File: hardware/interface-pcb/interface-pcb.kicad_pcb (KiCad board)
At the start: 2 copper layers, 90 x 75 mm, 102 parts, among them J1 Siedle bus Ta/Tb, J2 ext. 5V, Q1 IRFR120N, Q2 BC846B, Q3 BCP56-16, Q4 BCP56-16, Q5 BC846B, SW1 setup, U1 R-78CK5.0-0.5, U2 LM393, U3 ES8311, U4 MCP6002, U5 ESP32 D1 Mini

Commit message: Show the D1 Mini in the 3D view
The 3D view showed the empty sockets only, so the case design had no
module to work around. MK1 is a mechanical footprint locked on U5's
position that carries just a 3D model of the AZ-Delivery ESP32 D1 Mini:
no pads, not in the schematic, BOM or position files, footprint type
Unspecified. That makes it switchable: the 3D viewer's Unspecified
models toggle shows the board with or without it, and the STEP export
drops it with --no-unspecified. Putting the model into U5's own
footprint would instead need a footprint edit for every toggle.

tools/d1_mini_model.py builds the model from nominal dimensions (AZ-
Delivery's product page and photos): the board, the WROOM-32 with its
antenna at the edge, micro-USB, reset button, CP2104 and the male
headers, the top at about 15.3 mm above our board. The parameters take
the caliper measurements later. Both model scripts now share
tools/step_util.py for writing coloured STEP files.

DRC with schematic parity: 0 violations, 0 unconnected items, 0 parity
issues, as before.

Co-Authored-By: Claude Opus 5.5 <noreply@anthropic.com>
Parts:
- added MK1: ESP32 D1 Mini, 3D only, gateway:D1_Mini_ESP32_Module_3D, F.Cu at (116.0, 71.2)
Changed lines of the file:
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@@
+		)
+	)
+	(footprint "gateway:D1_Mini_ESP32_Module_3D"
+		(locked yes)
+		(layer "F.Cu")
+		(at 116 71.2)
+		(descr "3D model of the AZ-Delivery ESP32 D1 Mini plugged into the D1_Mini_ESP32_Socket footprint. Place at the socket footprint's origin. No pads, not in the schematic, BOM or position files; type Unspecified, so the 3D viewer can hide it and STEP export drops it with --no-unspecified.")
+		(tags "ESP32 D1 Mini 3D mechanical")
+		(property "Reference" "MK1"
+			(at 0 -22.5 0)
+			(layer "F.Fab")
+			(hide yes)
+			(effects
+				(font
+					(size 1 1)
+					(thickness 0.15)
+				)
+			)
+		)
+		(property "Value" "ESP32 D1 Mini, 3D only"
+			(at 0 21.5 0)
+			(layer "F.Fab")
+			(hide yes)
+			(effects
+				(font
+					(size 1 1)
+					(thickness 0.15)
+				)
+			)
+		)
+		(property "Datasheet" "https://www.az-delivery.de/en/products/esp32-d1-mini"
+			(at 0 0 0)
+			(layer "F.Fab")
+			(hide yes)
+			(effects
+				(font
+					(size 1.27 1.27)
+				)
+			)
+		)
+		(property "Description" "Mechanical: the D1 Mini module for the 3D view and the case design"
+			(at 0 0 0)
+			(layer "F.Fab")
+			(hide yes)
+			(effects
+				(font
+					(size 1.27 1.27)
+				)
+			)
+		)
+		(attr board_only exclude_from_pos_files exclude_from_bom)
+		(duplicate_pad_numbers_are_jumpers no)
+		(embedded_fonts no)
+		(model "${KIPRJMOD}/gateway.3dshapes/ESP32_D1_Mini_AZ-Delivery.step"
+			(offset
+				(xyz 0 0 0)
+			)
+			(scale
+				(xyz 1 1 1)
+			)
+			(rotate
+				(xyz 0 0 0)
+			)
 		)
 	)

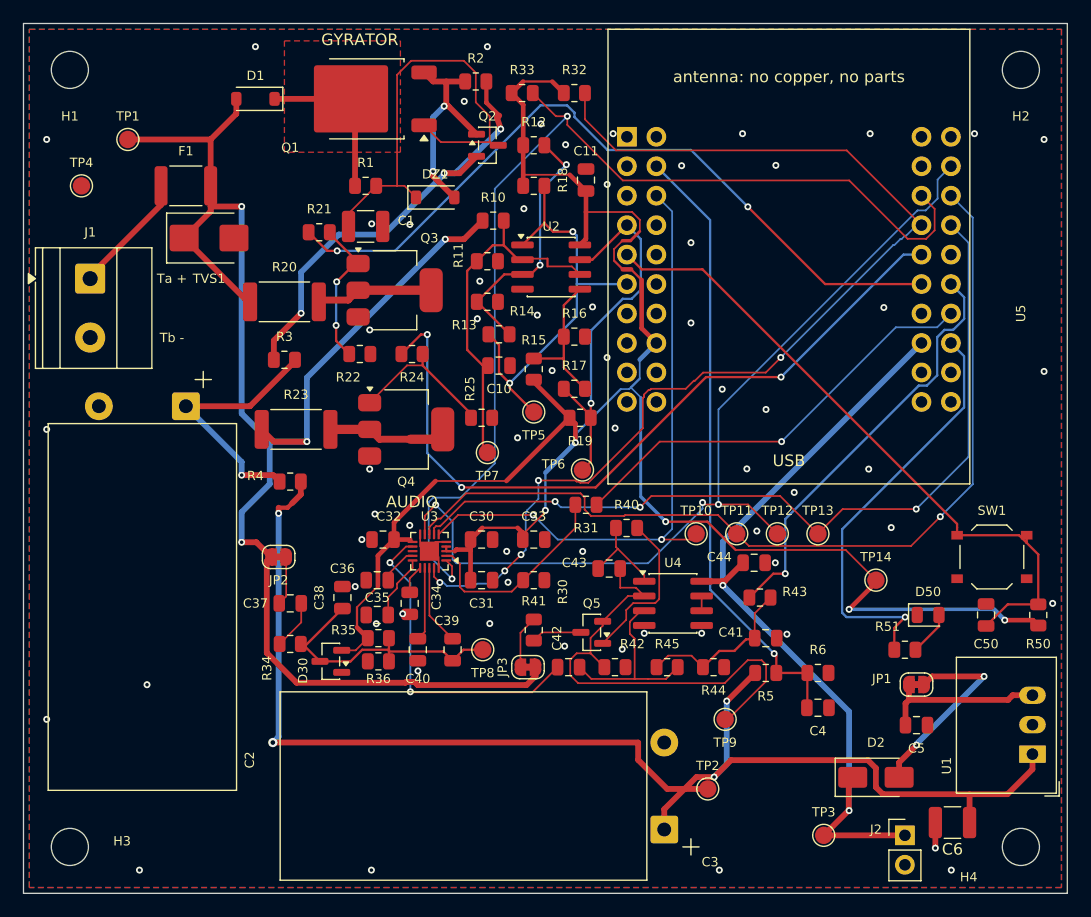
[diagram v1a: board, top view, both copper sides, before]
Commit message: Use 1000 uF / 35 V for C2 and C3
The 2200 uF / 50 V capacitors were the tallest parts after the D1 Mini.
Without load they sit about 4 V below the bus, 28 V while it rings at
32 V, so 35 V parts are enough; and smaller capacitors filter the Wi-Fi
bursts as well when R3 and R4 grow with them. C2 and C3 become
1000 uF / 35 V (13 x 20 mm, LCSC C10749), R3 and R4 33 and 39 ohms.

The decision comes before the bus measurements on purpose: if the bus
rings above 32 V, the 2200 uF / 50 V parts with 15 and 18 ohms go back
in, and the 16 mm footprint and model stay in the library for that.

Both variants get the change. A new lying footprint (5 mm pitch) and its
3D model replace the 16 mm ones on the boards; pad 1 stays put, pad 2
moves 2.5 mm closer and lands on C3's VOUT feed, which now runs straight
down to pad 1's track. gyrator.cir takes the new values: 3.2 s to 14 V,
VOUT 19.2 V, a 0.83 V dip during a frame, 130-170 kohm toward the bus
at speech frequencies.

ERC: no violations in both projects. DRC with schematic parity on the
D1 Mini board: 0 violations, 0 unconnected items, 0 parity issues. The
S3 board shows only the parity issues of its pending layout.

Co-Authored-By: Claude Opus 5.5 <noreply@anthropic.com>
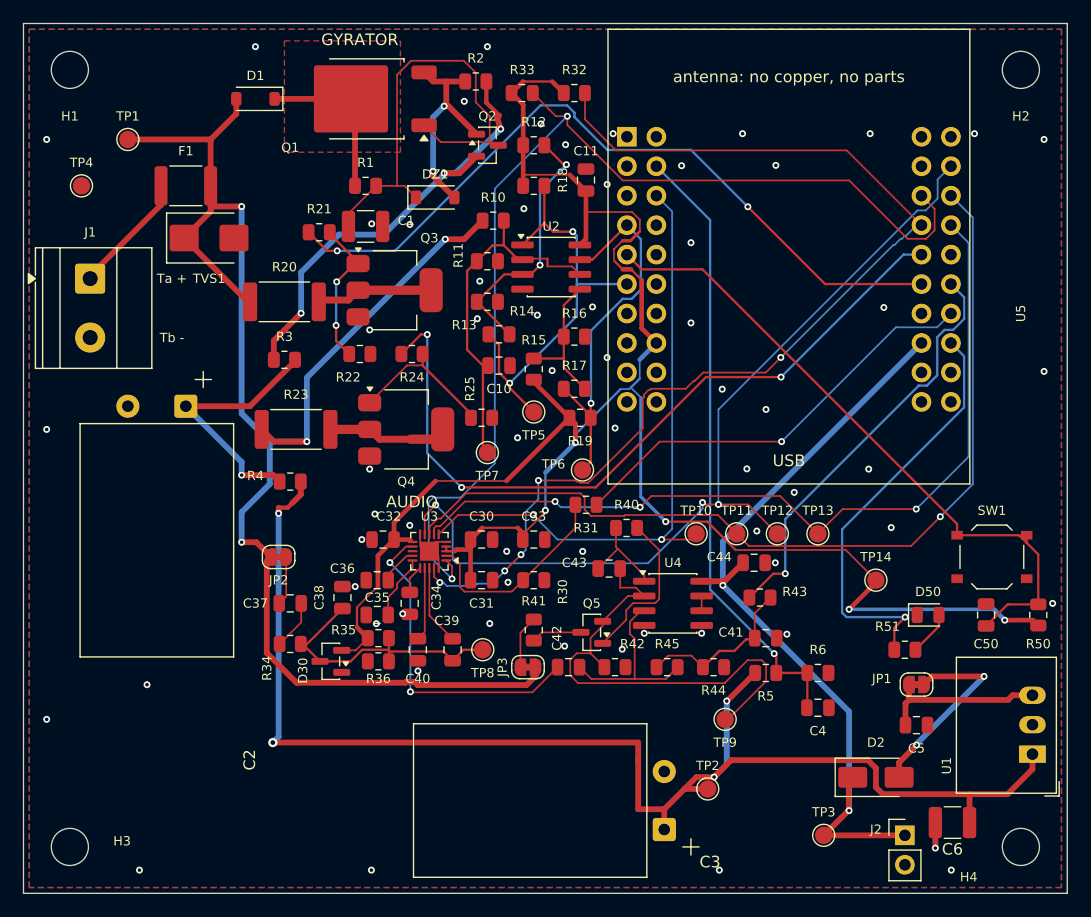
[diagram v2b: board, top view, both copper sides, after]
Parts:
- C2, C3: value 2200u 50V -> 1000u 35V; footprint gateway:CP_Radial_D16.0mm_P7.50mm_Lying -> gateway:CP_Radial_D13.0mm_P5.00mm_Lying
- R3: value 15 -> 33
- R4: value 18 -> 39
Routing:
- net /Bus input and power/VOUT: track 116.5 -> 118.0 mm
